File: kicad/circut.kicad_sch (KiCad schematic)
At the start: 17 parts, among them J1 AudioOut, J2 AudioOut, J3 I2C, J4 I2C, J5 Input1, J6 Input2, J7 VDD 5v, J8 Input3, J9 Input4, K1 G6K-2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

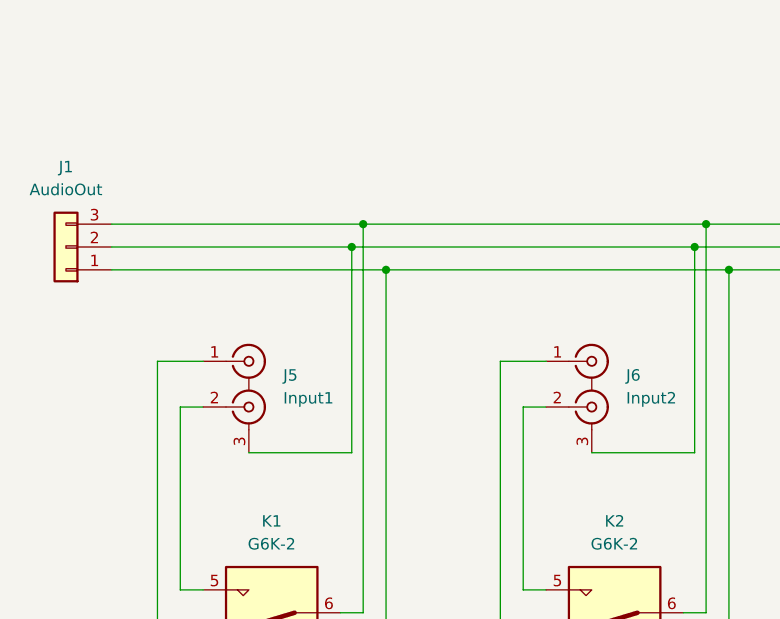
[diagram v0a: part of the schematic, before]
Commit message: Added cinch 2x2 symbol and footprint for 1x2 and 2x2
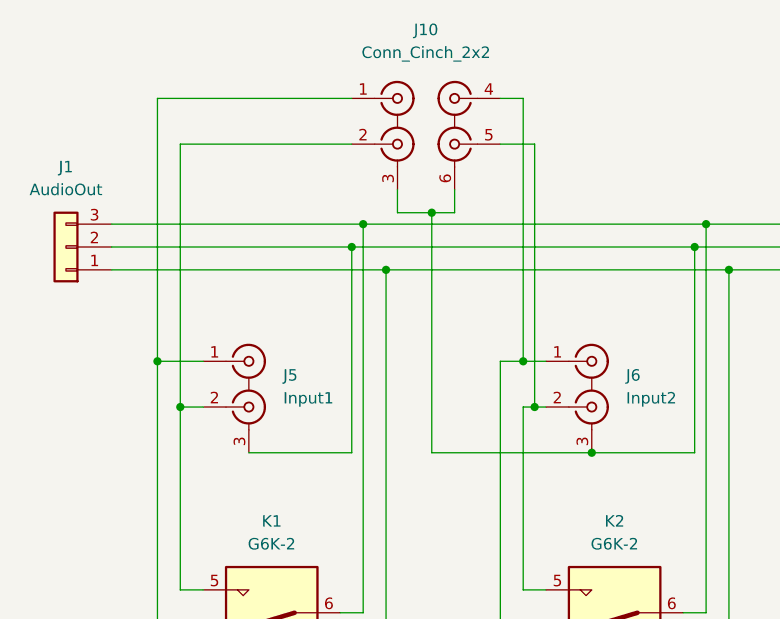
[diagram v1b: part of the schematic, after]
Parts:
- added J10: Conn_Cinch_2x2, Cinch-Sockets:cinch_2X2_Vertical, symbol Cinch:Conn_Cinch_2x2
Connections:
- net at J1.2 (Pin_2), J2.2 (Pin_2), J5.3 (EXT)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: now also J10.3 (EXT), J10.6 (EXT)
- net at J6.1 (IN1), K2.4: now also J10.4 (IN1)
- net at J6.2 (IN2), K2.5: now also J10.5 (IN2)
- net at J5.1 (IN1), K1.4: now also J10.1 (IN1)
- net at J5.2 (IN2), K1.5: now also J10.2 (IN2)
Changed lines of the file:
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@@
   (junction (at 127 35.56) (diameter 0) (color 0 0 0 0)
   )
+  (junction (at 27.94 50.8) (diameter 0) (color 0 0 0 0)
+  )
+  (junction (at 69.85 55.88) (diameter 0) (color 0 0 0 0)
+  )
   (junction (at 74.93 140.97) (diameter 0) (color 0 0 0 0)
   )
+  (junction (at 30.48 55.88) (diameter 0) (color 0 0 0 0)
+  )
   (junction (at 49.53 38.1) (diameter 0) (color 0 0 0 0)
   )
@@
   (junction (at 167.64 40.64) (diameter 0) (color 0 0 0 0)
   )
+  (junction (at 68.58 50.8) (diameter 0) (color 0 0 0 0)
+  )
   (junction (at 53.34 40.64) (diameter 0) (color 0 0 0 0)
   )
@@
   (junction (at 129.54 40.64) (diameter 0) (color 0 0 0 0)
   )
+  (junction (at 58.42 34.29) (diameter 0) (color 0 0 0 0)
+  )
   (junction (at 49.53 177.8) (diameter 0) (color 0 0 0 0)
   )
+  (junction (at 76.2 60.96) (diameter 0) (color 0 0 0 0)
+  )
   (junction (at 50.8 35.56) (diameter 0) (color 0 0 0 0)
   )
@@
     (stroke (width 0) (type default) (color 0 0 0 0))
   )
+  (wire (pts (xy 68.58 50.8) (xy 66.04 50.8))
+    (stroke (width 0) (type default) (color 0 0 0 0))
+  )
+  (wire (pts (xy 66.04 21.59) (xy 68.58 21.59))
+    (stroke (width 0) (type default) (color 0 0 0 0))
+  )
   (wire (pts (xy 91.44 40.64) (xy 129.54 40.64))
     (stroke (width 0) (type default) (color 0 0 0 0))
@@
     (stroke (width 0) (type default) (color 0 0 0 0))
   )
+  (wire (pts (xy 68.58 21.59) (xy 68.58 50.8))
+    (stroke (width 0) (type default) (color 0 0 0 0))
+  )
   (wire (pts (xy 46.99 111.76) (xy 147.32 111.76))
     (stroke (width 0) (type default) (color 0 0 0 0))
@@
     (stroke (width 0) (type default) (color 0 0 0 0))
   )
+  (wire (pts (xy 58.42 34.29) (xy 60.96 34.29))
+    (stroke (width 0) (type default) (color 0 0 0 0))
+  )
   (wire (pts (xy 163.83 38.1) (xy 173.99 38.1))
     (stroke (width 0) (type default) (color 0 0 0 0))
@@
     (stroke (width 0) (type default) (color 0 0 0 0))
   )
+  (wire (pts (xy 69.85 26.67) (xy 66.04 26.67))
+    (stroke (width 0) (type default) (color 0 0 0 0))
+  )
+  (wire (pts (xy 76.2 60.96) (xy 58.42 60.96))
+    (stroke (width 0) (type default) (color 0 0 0 0))
+  )
+  (wire (pts (xy 30.48 26.67) (xy 49.53 26.67))
+    (stroke (width 0) (type default) (color 0 0 0 0))
+  )
   (wire (pts (xy 147.32 55.88) (xy 144.78 55.88))
     (stroke (width 0) (type default) (color 0 0 0 0))
@@
     (stroke (width 0) (type default) (color 0 0 0 0))
   )
+  (wire (pts (xy 54.61 34.29) (xy 58.42 34.29))
+    (stroke (width 0) (type default) (color 0 0 0 0))
+  )
   (wire (pts (xy 44.45 177.8) (xy 49.53 177.8))
     (stroke (width 0) (type default) (color 0 0 0 0))
@@
     (stroke (width 0) (type default) (color 0 0 0 0))
   )
+  (wire (pts (xy 54.61 31.75) (xy 54.61 34.29))
+    (stroke (width 0) (type default) (color 0 0 0 0))
+  )
+  (wire (pts (xy 69.85 55.88) (xy 69.85 26.67))
+    (stroke (width 0) (type default) (color 0 0 0 0))
+  )
   (wire (pts (xy 52.07 161.29) (xy 54.61 161.29))
     (stroke (width 0) (type default) (color 0 0 0 0))
@@
     (stroke (width 0) (type default) (color 0 0 0 0))
   )
+  (wire (pts (xy 60.96 34.29) (xy 60.96 31.75))
+    (stroke (width 0) (type default) (color 0 0 0 0))
+  )
   (wire (pts (xy 22.86 38.1) (xy 49.53 38.1))
     (stroke (width 0) (type default) (color 0 0 0 0))
@@
     (stroke (width 0) (type default) (color 0 0 0 0))
   )
-  (wire (pts (xy 71.12 55.88) (xy 68.58 55.88))
+  (wire (pts (xy 71.12 55.88) (xy 69.85 55.88))
     (stroke (width 0) (type default) (color 0 0 0 0))
   )
@@
     (stroke (width 0) (type default) (color 0 0 0 0))
   )
+  (wire (pts (xy 27.94 21.59) (xy 27.94 50.8))
+    (stroke (width 0) (type default) (color 0 0 0 0))
+  )
   (wire (pts (xy 48.26 88.9) (xy 53.34 88.9))
     (stroke (width 0) (type default) (color 0 0 0 0))
@@
     (stroke (width 0) (type default) (color 0 0 0 0))
   )
+  (wire (pts (xy 30.48 55.88) (xy 30.48 26.67))
+    (stroke (width 0) (type default) (color 0 0 0 0))
+  )
   (wire (pts (xy 147.32 50.8) (xy 142.24 50.8))
     (stroke (width 0) (type default) (color 0 0 0 0))
@@
     (stroke (width 0) (type default) (color 0 0 0 0))
   )
-  (wire (pts (xy 71.12 50.8) (xy 66.04 50.8))
+  (wire (pts (xy 71.12 50.8) (xy 68.58 50.8))
     (stroke (width 0) (type default) (color 0 0 0 0))
   )
@@
     (stroke (width 0) (type default) (color 0 0 0 0))
   )
+  (wire (pts (xy 58.42 60.96) (xy 58.42 34.29))
+    (stroke (width 0) (type default) (color 0 0 0 0))
+  )
+  (wire (pts (xy 69.85 55.88) (xy 68.58 55.88))
+    (stroke (width 0) (type default) (color 0 0 0 0))
+  )
   (wire (pts (xy 44.45 109.22) (xy 44.45 128.27))
     (stroke (width 0) (type default) (color 0 0 0 0))
@@
   )
   (wire (pts (xy 20.32 160.02) (xy 20.32 163.83))
+    (stroke (width 0) (type default) (color 0 0 0 0))
+  )
+  (wire (pts (xy 49.53 21.59) (xy 27.94 21.59))
     (stroke (width 0) (type default) (color 0 0 0 0))
   )
@@
     (pin "1")
     (pin "2")
+  )
+  (symbol (lib_id "Cinch:Conn_Cinch_2x2") (at 54.61 24.13 0) (unit 1)
+    (in_bom yes) (on_board yes) (fields_autoplaced)
+    (property "Reference" "J10" (id 0) (at 57.785 13.97 0))
+    (property "Value" "Conn_Cinch_2x2" (id 1) (at 57.785 16.51 0))
+    (property "Footprint" "Cinch-Sockets:cinch_2X2_Vertical" (id 2) (at 54.61 26.67 0)
+      (effects (font (size 1.27 1.27)) hide)
+    )
+    (property "Datasheet" " ~" (id 3) (at 54.61 26.67 0)
+      (effects (font (size 1.27 1.27)) hide)
+    )
+    (pin "1")
+    (pin "2")
+    (pin "3")
+    (pin "4")
+    (pin "5")
+    (pin "6")
   )
   (symbol (lib_id "Connector_Generic:Conn_01x02") (at 93.98 154.94 270) (unit 1)
@@
       (reference "J9") (unit 1) (value "Input4") (footprint "Connector:Banana_Jack_3Pin")
     )
+    (path "/a0482958-f664-480d-a7f6-9885a14ac5cf"
+      (reference "J10") (unit 1) (value "Conn_Cinch_2x2") (footprint "Cinch-Sockets:cinch_2X2_Vertical")
+    )
     (path "/2cbe4c67-10a2-4fb4-91aa-de1bb6bc0b41"

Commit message: Second PCB Layout - Much smaller. Changed relais wireing.
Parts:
- removed J5: Input1, Connector:Banana_Jack_3Pin, symbol Connector:Conn_Coaxial_x2
- removed J6: Input2, Connector:Banana_Jack_3Pin, symbol Connector:Conn_Coaxial_x2
- removed J8: Input3, Connector:Banana_Jack_3Pin, symbol Connector:Conn_Coaxial_x2
- removed J9: Input4, Connector:Banana_Jack_3Pin, symbol Connector:Conn_Coaxial_x2
- added J5: Input 1/2, Cinch-Sockets:cinch_2X2_Vertical, symbol Cinch:Conn_Cinch_2x2
- added JP4: Audio to Control GND, Connector_PinSocket_1.00mm:PinSocket_1x02_P1.00mm_Vertical, symbol Jumper:Jumper_2_Open
- J10: value Conn_Cinch_2x2 -> Input 1/2
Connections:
- net GND: now also JP4.2 (B); no longer K1.8, K2.8, K3.8, K4.8
- net VDD: now also K1.8, K2.8, K3.8, K4.8
- net GND1: now reaches J1.2 (Pin_2), J10.3 (EXT), J10.6 (EXT), J2.2 (Pin_2)
- net GND1: now also J5.3 (EXT), J5.6 (EXT), JP4.1 (A)
- net at K3.4: now also J1.3 (Pin_3), J2.1 (Pin_1), K1.4, K2.3, K4.3
- net at K3.5: now also J1.1 (Pin_1), J2.3 (Pin_3), K1.5, K2.6, K4.6
- net at K4.4: now also J5.5 (IN2)
- net at K4.5: now also J5.4 (IN1)
- net at K2.4: now also J10.5 (IN2); no longer J10.4 (IN1)
- net at K2.5: now also J10.4 (IN1); no longer J10.5 (IN2)
- net at J10.1 (IN1): now also K1.6; no longer K1.4
- net at J10.2 (IN2): now also K1.3; no longer K1.5
- new net: J5.2 (IN2), K3.3
- new net: J5.1 (IN1), K3.6
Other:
- title: (none) -> Open PreAmp 4 Channel Input Selector
- moved on the sheet: J1, J10, J2, J3, J4, J7, JP1, JP2, JP3, K1, K2, K3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
